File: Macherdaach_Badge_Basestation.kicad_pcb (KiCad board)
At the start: 2 copper layers, 50 x 100 mm, 4 parts, among them J1 Conn_01x04_Male, J3 AVR-ISP-HEADER, SW3 ON_OFF_Switch

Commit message: no idea what i did there
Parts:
- removed SW3: ON_OFF_Switch, ESP101:ESP101
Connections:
- J1 pad 2: /RX -> /D7
- J1 pad 3: /TX -> /D8
- J3 pad 2: Net-(J3-Pad2) -> +3V3
- MOD1 pad 18: /TX -> (no net)
- MOD1 pad 19: /RX -> (no net)
- MOD1 pad 20: (no net) -> /D8
- MOD1 pad 21: (no net) -> /D7
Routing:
- net /TX: track 49.3 -> 0.00 mm
- net /RX: track 49.3 -> 0.00 mm
- net /D8: track 0.00 -> 44.3 mm
- net /D7: track 0.00 -> 44.3 mm
- net Net-(J3-Pad2): track 37.6 -> 0.00 mm
- net +3V3: track 98.4 -> 134.2 mm
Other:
- board text added: "Badge vor dem Einstecken ausschalten!"
- board text removed: "AN"
- board text removed: "AUS"
- board text removed: "Badge vor dem Einstecken ausschalten"

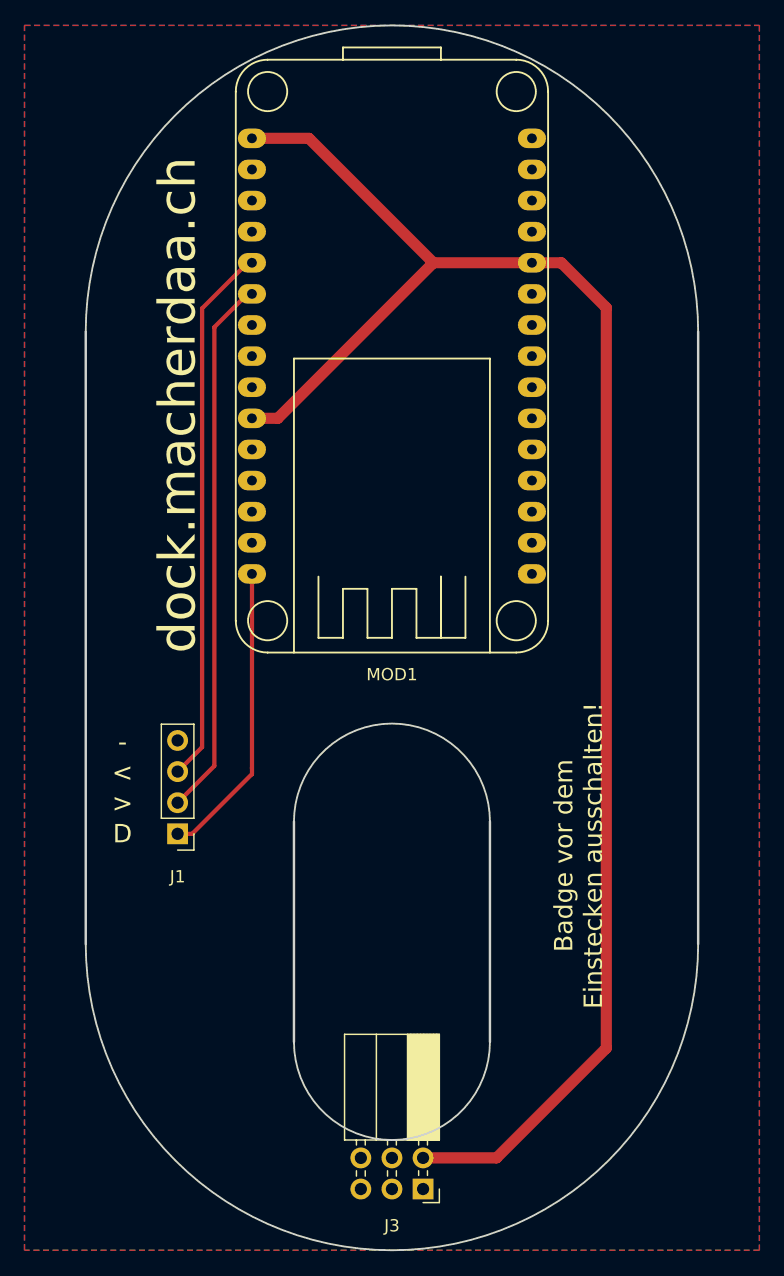
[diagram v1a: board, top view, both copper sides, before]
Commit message: changed NodeMCU board v1.0 to v0.1 which is bigger
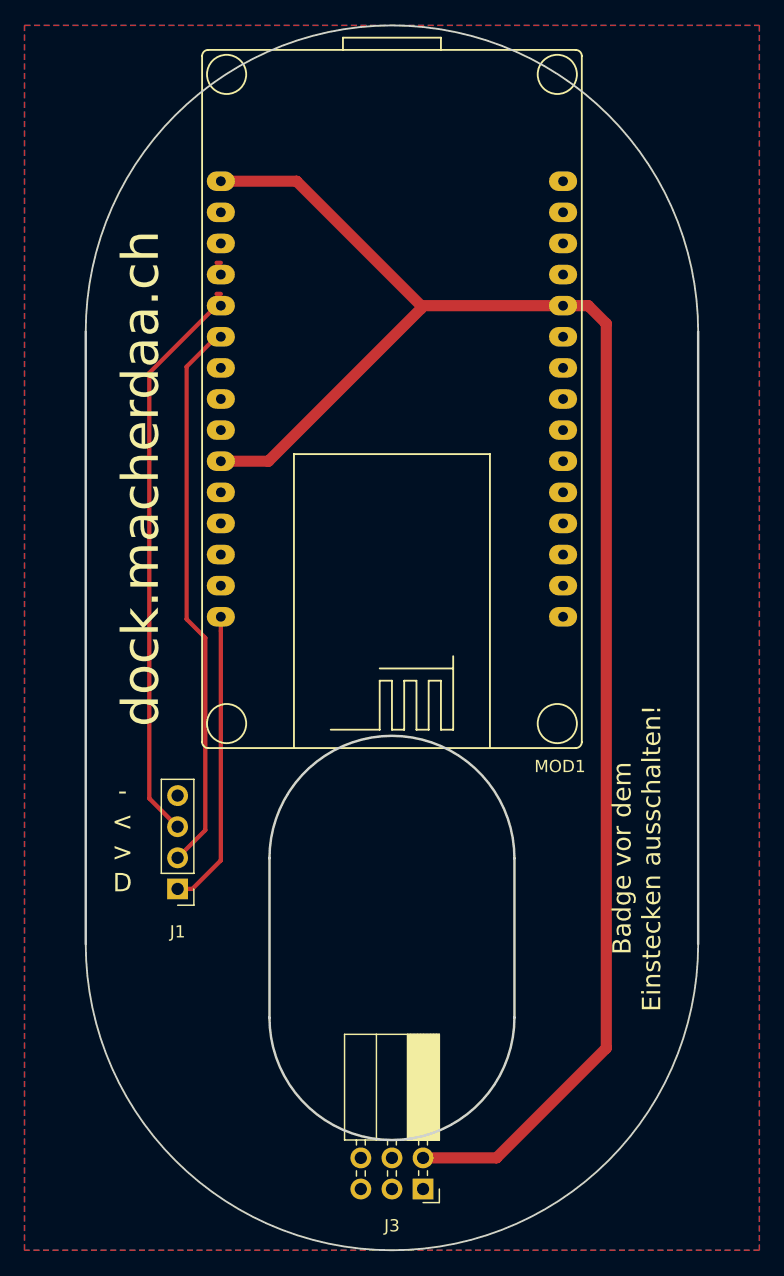
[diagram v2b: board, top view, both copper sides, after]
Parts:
- MOD1: footprint NodeMCU:NodeMCU -> NodeMCU:NodeMCU_v0.1
- moved J1 4.50 mm to (107.5, 120.5)
- moved MOD1 3.50 mm to (125.0, 80.5)
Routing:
- net /D8: track 44.3 -> 46.5 mm
- net +3V3: track 134.2 -> 135.9 mm
- net /D7: track 44.3 -> 45.5 mm
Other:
- outline, holes or cut-outs redrawn

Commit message: Adjustet some componenets and reanotation
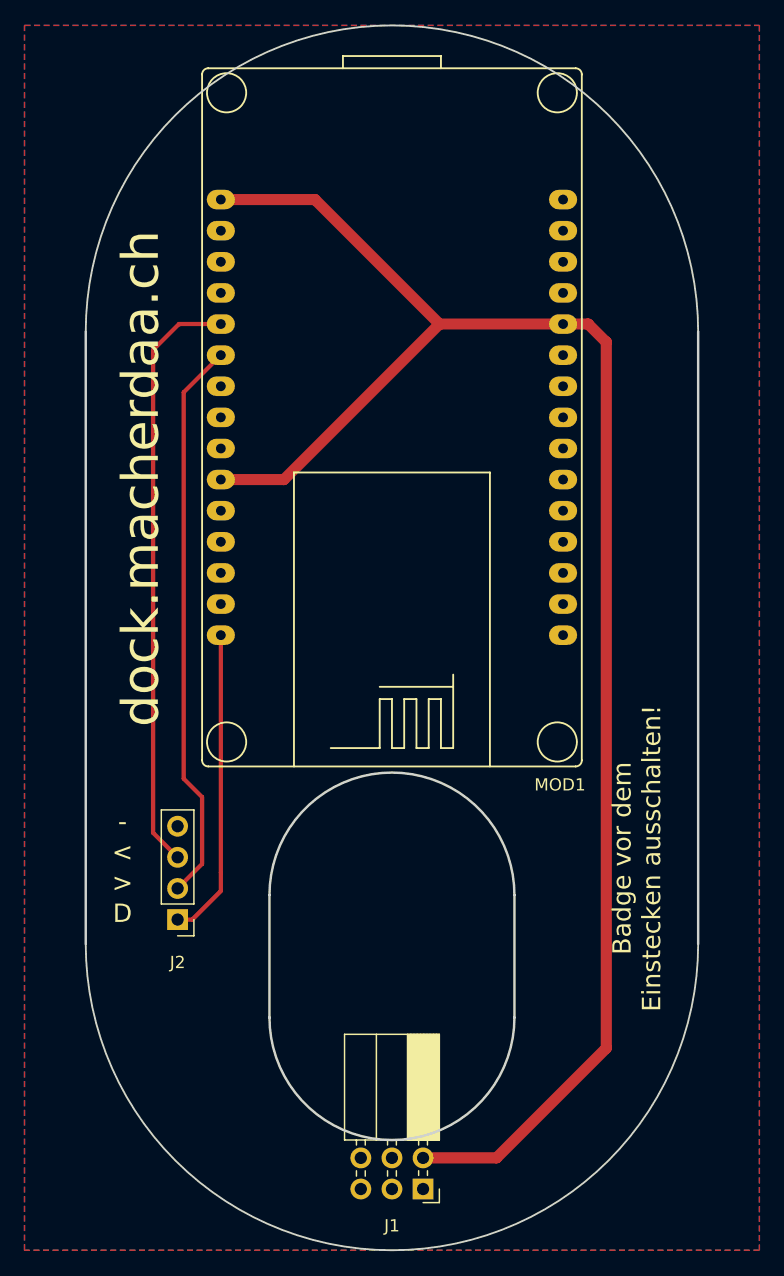
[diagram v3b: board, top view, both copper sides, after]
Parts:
- moved J2 2.50 mm to (107.5, 123.0)
- moved MOD1 1.50 mm to (125.0, 82.0)
- renumbered J3 to J1, J1 to J2
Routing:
- net /D8: track 46.5 -> 48.7 mm
- net /D0: track 24.4 -> 25.4 mm
- net /D7: track 45.5 -> 46.2 mm
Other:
- outline, holes or cut-outs redrawn
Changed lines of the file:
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@@
     (thickness 1.6)
     (drawings 17)
-    (tracks 27)
+    (tracks 23)
     (zones 0)
     (modules 3)
@@
       (drillshape 0)
       (scaleselection 1)
-      (outputdirectory "Export/Gerber/v1"))
+      (outputdirectory "Export/Gerber/v2/"))
   )
   (net 0 "")
@@
   )
   (module Connector_PinHeader_2.54mm:PinHeader_1x04_P2.54mm_Vertical (layer F.Cu)
-    (at 107.5 120.5 180)
+    (at 107.5 123 180)
     (descr "Through hole straight pin header, 1x04, 2.54mm pitch, single row")
     (tags "Through hole pin header THT 1x04 2.54mm single row")
-    (fp_text reference J1 (at 0 -3.5 180) (layer F.SilkS)
+    (fp_text reference J2 (at 0 -3.5 180) (layer F.SilkS)
       (effects (font (size 1 1) (thickness 0.15)))
     )
@@
     (descr "Through hole angled socket strip, 2x03, 2.54mm pitch, 8.51mm socket length, double cols (from Kicad 4.0.7), script generated")
     (tags "Through hole angled socket strip THT 2x03 2.54mm double row")
-    (fp_text reference J3 (at 3 2.54) (layer F.SilkS)
+    (fp_text reference J1 (at 3 2.54) (layer F.SilkS)
       (effects (font (size 1 1) (thickness 0.15)))
     )
@@
   )
   (module NodeMCU:NodeMCU_v0.1 (layer F.Cu)
-    (at 125 80.5 180)
+    (at 125 82 180)
     (fp_text reference MOD1 (at -13.716 -30) (layer F.SilkS)
       (effects (font (size 1 1) (thickness 0.15)))
@@
     (effects (font (size 1.5 1.5) (thickness 0.3)))
   )
-  (gr_text D (at 103 120) (layer F.SilkS)
-    (effects (font (size 1.5 1.5) (thickness 0.3)))
-  )
-  (gr_text > (at 103 117.5) (layer F.SilkS)
-    (effects (font (size 1.5 1.5) (thickness 0.3)))
-  )
-  (gr_text < (at 103 115) (layer F.SilkS)
-    (effects (font (size 1.5 1.5) (thickness 0.3)))
-  )
-  (gr_text - (at 103 112.5) (layer F.SilkS)
+  (gr_text D (at 103 122.5) (layer F.SilkS)
+    (effects (font (size 1.5 1.5) (thickness 0.3)))
+  )
+  (gr_text > (at 103 120) (layer F.SilkS)
+    (effects (font (size 1.5 1.5) (thickness 0.3)))
+  )
+  (gr_text < (at 103 117.5) (layer F.SilkS)
+    (effects (font (size 1.5 1.5) (thickness 0.3)))
+  )
+  (gr_text - (at 103 115) (layer F.SilkS)
     (effects (font (size 1.5 1.5) (thickness 0.3)))
   )
   (gr_arc (start 125 131) (end 115 131) (angle -180) (layer Edge.Cuts) (width 0.2))
-  (gr_arc (start 125 118) (end 135 118) (angle -180) (layer Edge.Cuts) (width 0.2))
-  (gr_line (start 135 118) (end 135 131) (layer Edge.Cuts) (width 0.2))
-  (gr_line (start 115 131) (end 115 118) (layer Edge.Cuts) (width 0.2))
+  (gr_arc (start 125 121) (end 135 121) (angle -180) (layer Edge.Cuts) (width 0.2))
+  (gr_line (start 135 121) (end 135 131) (layer Edge.Cuts) (width 0.2))
+  (gr_line (start 115 131) (end 115 121) (layer Edge.Cuts) (width 0.2))
   (gr_circle (center 125 65) (end 130 65) (layer B.SilkS) (width 0.2))
   (gr_circle (center 109 135) (end 114 135) (layer B.SilkS) (width 0.2))
@@
   (gr_line (start 150 75) (end 150 125) (layer Edge.Cuts) (width 0.2))
   (gr_line (start 100 125) (end 100 75) (layer Edge.Cuts) (width 0.2))
-  (segment (start 110.68 71.92) (end 111.03 71.92) (width 0.35) (layer F.Cu) (net 5))
-  (segment (start 110.68 69.38) (end 111.03 69.38) (width 0.35) (layer F.Cu) (net 0))
-  (segment (start 111.03 99.43) (end 111.03 98.28) (width 0.35) (layer F.Cu) (net 1))
-  (segment (start 111.03 118.17) (end 111.03 99.43) (width 0.35) (layer F.Cu) (net 1))
-  (segment (start 108.7 120.5) (end 111.03 118.17) (width 0.35) (layer F.Cu) (net 1))
-  (segment (start 107.5 120.5) (end 108.7 120.5) (width 0.35) (layer F.Cu) (net 1))
+  (segment (start 108.7 123) (end 107.5 123) (width 0.35) (layer F.Cu) (net 1))
+  (segment (start 111.03 120.67) (end 108.7 123) (width 0.35) (layer F.Cu) (net 1))
+  (segment (start 111.03 119.17) (end 111.03 99.78) (width 0.35) (layer F.Cu) (net 1))
+  (segment (start 111.03 120.67) (end 111.03 119.17) (width 0.35) (layer F.Cu) (net 1))
+  (segment (start 142.5 133.5) (end 133.54 142.46) (width 0.91) (layer F.Cu) (net 3))
   (segment (start 133.54 142.46) (end 127.54 142.46) (width 0.91) (layer F.Cu) (net 3))
-  (segment (start 142.5 133.5) (end 133.54 142.46) (width 0.91) (layer F.Cu) (net 3))
-  (segment (start 142.5 74.35) (end 142.5 133.5) (width 0.91) (layer F.Cu) (net 3))
-  (segment (start 141.03 72.88) (end 142.5 74.35) (width 0.91) (layer F.Cu) (net 3))
-  (segment (start 138.97 72.88) (end 141.03 72.88) (width 0.91) (layer F.Cu) (net 3))
-  (segment (start 138.97 72.88) (end 127.38 72.88) (width 0.91) (layer F.Cu) (net 3))
-  (segment (start 117.22 62.72) (end 111.03 62.72) (width 0.91) (layer F.Cu) (net 3))
-  (segment (start 127.38 72.88) (end 117.22 62.72) (width 0.91) (layer F.Cu) (net 3))
-  (segment (start 127.38 72.88) (end 127.38 73.12) (width 0.91) (layer F.Cu) (net 3))
-  (segment (start 114.92 85.58) (end 111.03 85.58) (width 0.91) (layer F.Cu) (net 3))
-  (segment (start 127.38 73.12) (end 114.92 85.58) (width 0.91) (layer F.Cu) (net 3))
-  (segment (start 109.76 115.7) (end 107.5 117.96) (width 0.35) (layer F.Cu) (net 4))
-  (segment (start 109.76 100) (end 109.76 115.7) (width 0.35) (layer F.Cu) (net 4))
-  (segment (start 108.236 98.476) (end 109.76 100) (width 0.35) (layer F.Cu) (net 4))
-  (segment (start 110.68 75.42) (end 111.03 75.42) (width 0.35) (layer F.Cu) (net 4))
-  (segment (start 108.236 77.864) (end 110.68 75.42) (width 0.35) (layer F.Cu) (net 4))
-  (segment (start 108.236 98.476) (end 108.236 77.864) (width 0.35) (layer F.Cu) (net 4))
-  (segment (start 105.188 113.108) (end 107.5 115.42) (width 0.35) (layer F.Cu) (net 5))
-  (segment (start 110.68 72.88) (end 111.03 72.88) (width 0.35) (layer F.Cu) (net 5))
-  (segment (start 105.188 78.372) (end 110.68 72.88) (width 0.35) (layer F.Cu) (net 5))
-  (segment (start 105.188 113.108) (end 105.188 78.372) (width 0.35) (layer F.Cu) (net 5))
+  (segment (start 142.5 75.85) (end 142.5 133.5) (width 0.91) (layer F.Cu) (net 3))
+  (segment (start 141.03 74.38) (end 142.5 75.85) (width 0.91) (layer F.Cu) (net 3))
+  (segment (start 138.97 74.38) (end 141.03 74.38) (width 0.91) (layer F.Cu) (net 3))
+  (segment (start 138.97 74.38) (end 128.88 74.38) (width 0.91) (layer F.Cu) (net 3))
+  (segment (start 118.72 64.22) (end 111.03 64.22) (width 0.91) (layer F.Cu) (net 3))
+  (segment (start 128.88 74.38) (end 118.72 64.22) (width 0.91) (layer F.Cu) (net 3))
+  (segment (start 116.18 87.08) (end 111.03 87.08) (width 0.91) (layer F.Cu) (net 3))
+  (segment (start 128.88 74.38) (end 116.18 87.08) (width 0.91) (layer F.Cu) (net 3))
+  (segment (start 108 111.5) (end 108 79.95) (width 0.35) (layer F.Cu) (net 4))
+  (segment (start 109.5 113) (end 108 111.5) (width 0.35) (layer F.Cu) (net 4))
+  (segment (start 107.5 120.46) (end 109.5 118.46) (width 0.35) (layer F.Cu) (net 4))
+  (segment (start 109.5 118.46) (end 109.5 113) (width 0.35) (layer F.Cu) (net 4))
+  (segment (start 108 79.95) (end 111.03 76.92) (width 0.35) (layer F.Cu) (net 4))
+  (segment (start 107.62 74.38) (end 111.03 74.38) (width 0.35) (layer F.Cu) (net 5))
+  (segment (start 105.5 76.5) (end 107.62 74.38) (width 0.35) (layer F.Cu) (net 5))
+  (segment (start 107.5 117.92) (end 105.5 115.92) (width 0.35) (layer F.Cu) (net 5))
+  (segment (start 105.5 115.92) (end 105.5 76.5) (width 0.35) (layer F.Cu) (net 5))
   (zone (net 2) (net_name GND) (layer F.Cu) (hatch edge 0.508)
     (connect_pads (clearance 0.508))
